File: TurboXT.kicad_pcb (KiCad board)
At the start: 2 copper layers, 74.3 x 43.8 mm, 27 parts, among them J1 8284 Socket, J2 HRQDMA, J3 DMAWAIT, J4 VCC, J5 GND, J6 Turbo LED, J7 Reset, SW1 TURBO SWITCH, U1 8284, U2 74LS92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

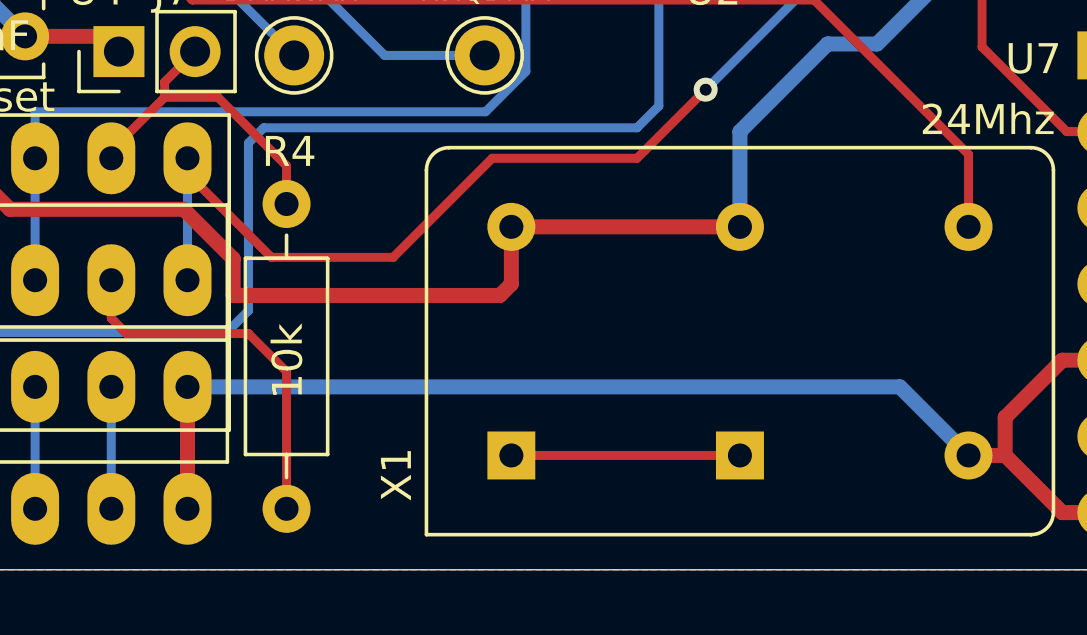
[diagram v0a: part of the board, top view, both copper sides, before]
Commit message: Add cap for deboucing
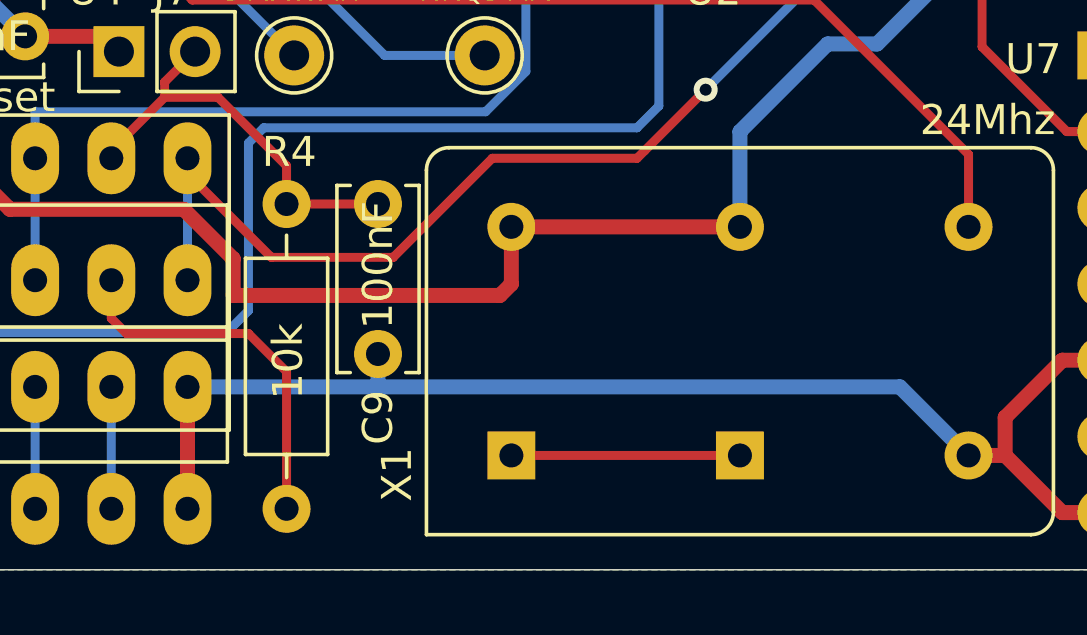
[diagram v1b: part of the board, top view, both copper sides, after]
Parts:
- added C9: 100nF, Capacitor_THT:C_Disc_D6.0mm_W2.5mm_P5.00mm, F.Cu at (75.2, 95.8)
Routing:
- net /~RES: track 11.0 -> 14.0 mm
- net GND: track 217.6 -> 218.7 mm
